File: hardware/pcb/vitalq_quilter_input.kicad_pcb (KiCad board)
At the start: 6 copper layers, 46 x 70 mm, 292 parts, among them J1 USB-C, J10 Optical tail pads, J11 Sweat site, J12 FH12-14S, J13 MX ECG pads, J2 LiPo pads, J3 FSR pads, J5 ECG pads, J6 EDA pads, J7 Chest bioZ, J8 TC2030, J9 I2C tail pads, Q1 CSD13380F3T, Q2 CSD13380F3T, Q3 BC847BS,115, Q4 CSD13380F3T, SW1 TS-1088, SW2 TS-1088, U1 ESP32-S3-MINI-1-N4R2, U10 AS7341-DLGM, U11 TMP117AIDRVR, U12 MLX90632SLD-DCB-100-SP, U13 BME280, U14 LSM6DSV80XTR, U15 TPS61240YFFR, U16 SFH 7072, U17 MAX17048G+T10, U18 W25Q512JVEIQ, U19 TCA6408ARSVR, U2 BQ25170DSGR, U20 TMP117AIDRVR, U21 USBLC6-2SC6, U22 MAX86178ENJ+, U23 SHT45-AD1B, U24 RV-3028-C7, U25 IM69D130, U3 TPS63802DLAR, U4 TPS7A2018PDBVR, U5 CP2102N-A02-GQFN28R, U6 AFE4900YZR, U7 AD5940BCBZ-RL7, U8 ADS1292RIRSMT, U9 PCA9306DCUR

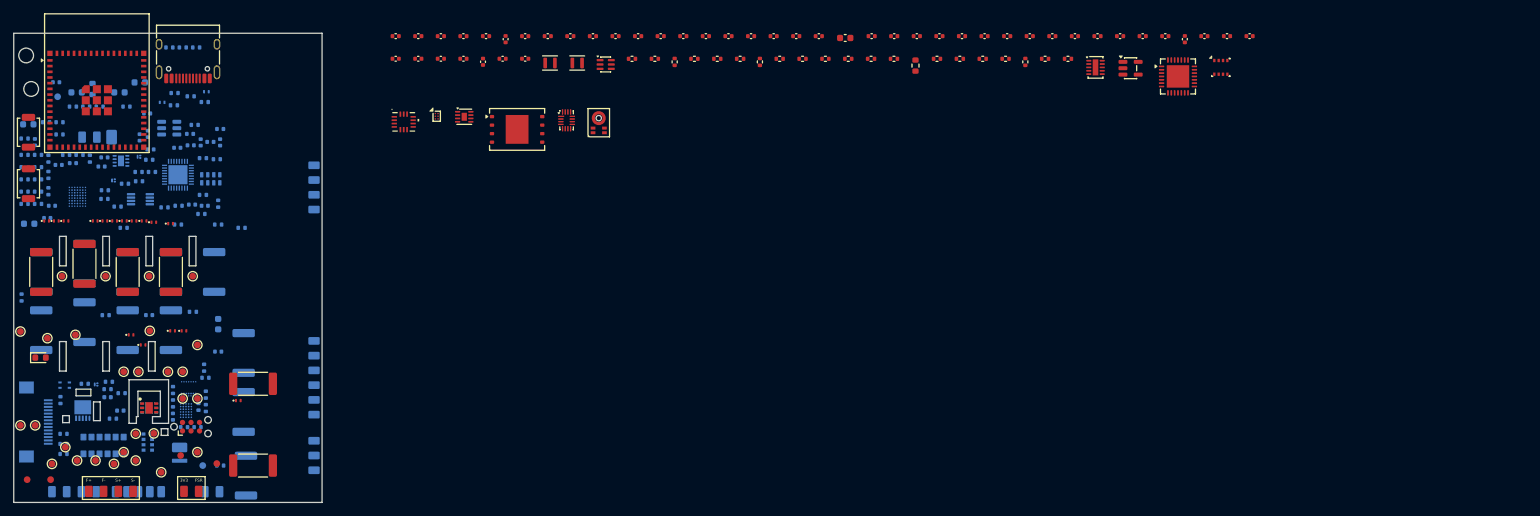
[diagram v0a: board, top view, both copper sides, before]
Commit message: Reduce Quilter lock set: 87 fixed parts, 205 parked off-board
Locked = skin sensor cluster (U6 AFE4900, U10 AS7341, U11+U20 TMP117
pair, U12 MLX90632, U16 SFH7072, U22 MAX86178, U23 SHT45, D10-D12 optics),
HV corridor (R32-36, R76-83, R118-122, D1-D3/D6-D9/D21-D30), all J* pads
and TP1-28, and U1 ESP32. Everything else incl. passives, regulators,
ESD, buttons, fiducials parked east of the outline for Quilter to place.

Generated with [Devin](https://devin.ai)

Co-Authored-By: Devin <158243242+devin-ai-integration[bot]@users.noreply.github.com>
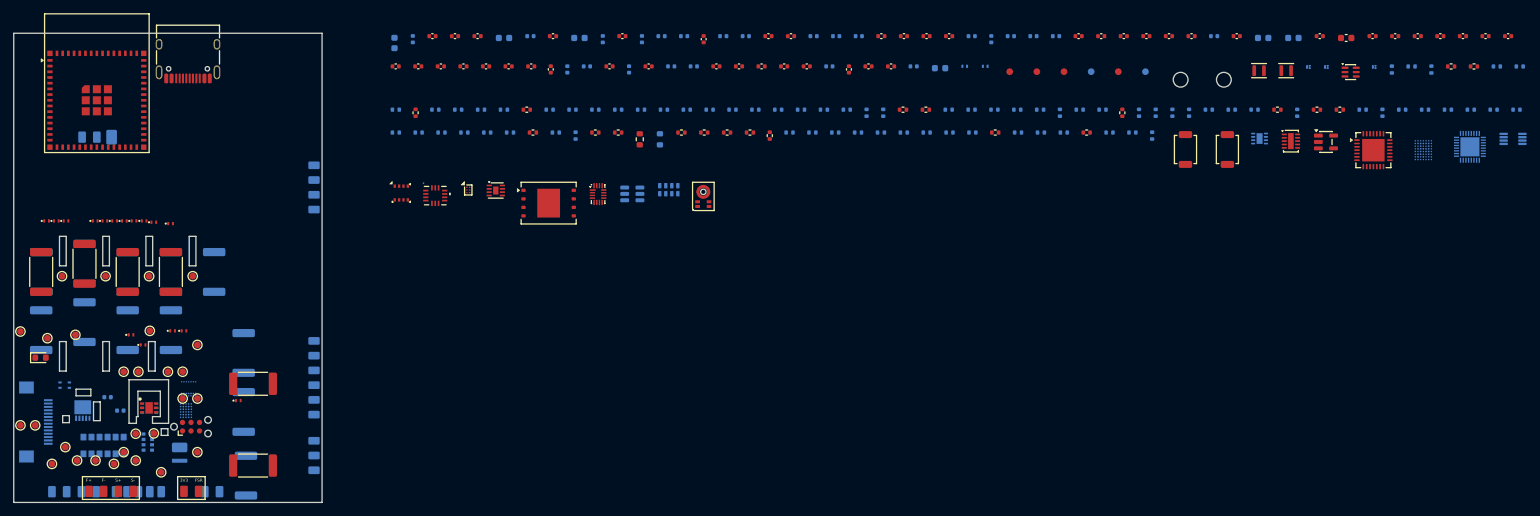
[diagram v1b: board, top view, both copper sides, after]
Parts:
- moved R2 207.4 mm to (208.6, -3.04)
- moved R3 206.8 mm to (211.5, -2.58)
- moved R7 206.3 mm to (221.3, -3.04)
- moved U9 205.0 mm to (223.7, 7.76)
- moved R67 204.9 mm to (204.2, 3.87)
- moved R73 201.2 mm to (224.2, 3.40)
- moved U7 200.9 mm to (210.3, 9.45)
- moved R72 197.0 mm to (220.8, 3.40)
- moved Q4 196.5 mm to (203.0, -2.97)
- moved R68 195.8 mm to (207.2, 3.40)
- moved R8 194.9 mm to (224.7, -3.04)
- moved U8 192.8 mm to (217.3, 8.95)
- moved R69 186.3 mm to (210.6, 3.40)
- moved R70 184.3 mm to (214.0, 3.40)
- moved R71 184.2 mm to (217.4, 3.40)
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
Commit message: Unlock TP1-28 test pads, park off-board for Quilter (59 locked / 233 parked)
Generated with [Devin](https://devin.ai)

Co-Authored-By: Devin <158243242+devin-ai-integration[bot]@users.noreply.github.com>
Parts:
- moved TP12 225.2 mm to (224.4, 8.10)
- moved TP11 223.9 mm to (220.9, 8.10)
- moved TP10 217.0 mm to (217.3, 8.10)
- moved TP7 197.7 mm to (206.7, 8.10)
- moved TP9 190.3 mm to (213.8, 8.10)
- moved TP6 190.0 mm to (203.1, 8.10)
- moved TP8 189.0 mm to (210.2, 8.10)
- moved TP5 187.5 mm to (199.6, 8.10)
- moved TP4 174.3 mm to (196.0, 8.10)
- moved TP2 173.8 mm to (188.9, 8.10)
- moved TP3 172.9 mm to (192.5, 8.10)
- moved TP1 172.4 mm to (185.4, 8.10)
- moved TP28 107.5 mm to (110.3, 15.6)
- moved TP25 100.9 mm to (99.7, 15.6)
- moved U17 99.9 mm to (171.9, 15.3)
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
